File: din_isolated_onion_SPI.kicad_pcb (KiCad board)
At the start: 2 copper layers, 32.5 x 40.5 mm, 38 parts, among them J1 Conn_01x16, J2 Conn_01x16, J3 Conn_01x10, J4 Test_Power_Bridge, U1 Omega2+, U2 SI8661AB-B-IS1, U3 TPL5010-Q1, U4 74LVC125, U5 NL7SZ19

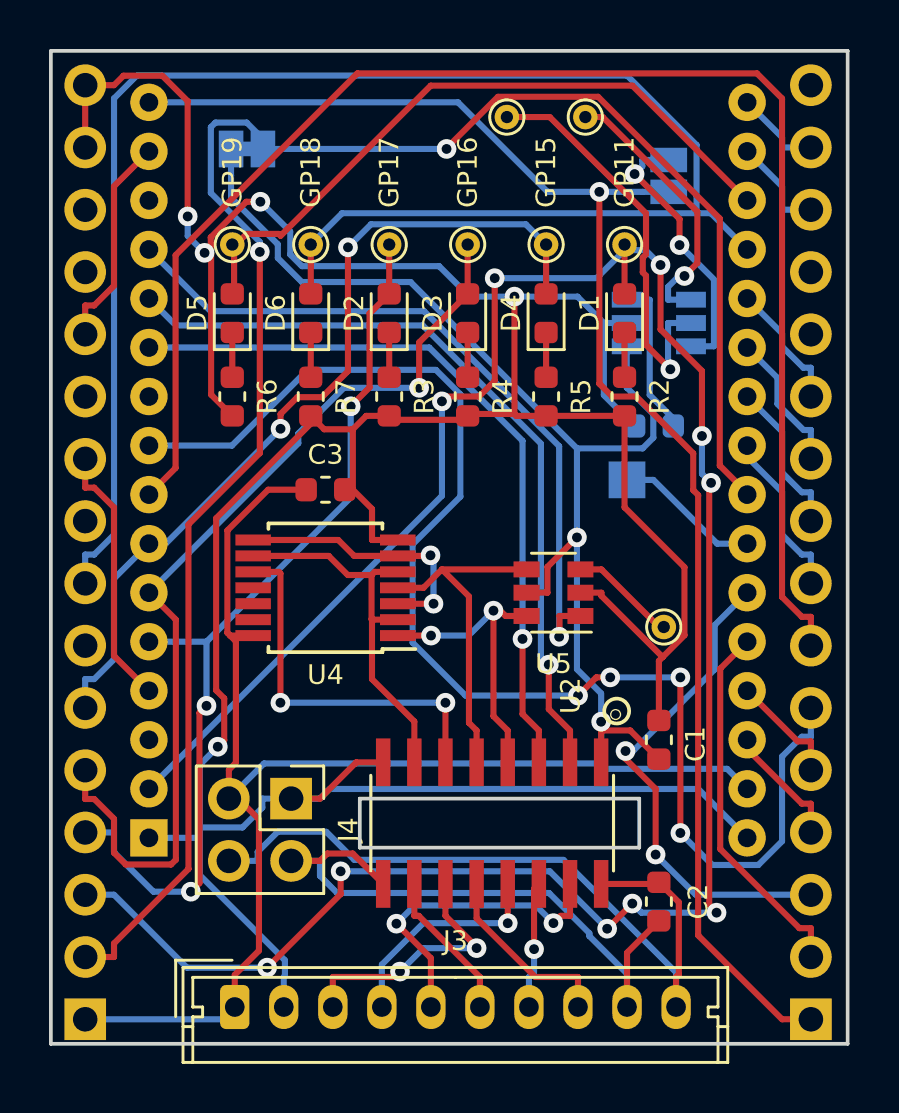
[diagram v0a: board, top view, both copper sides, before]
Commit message: Complete route with x4 layers
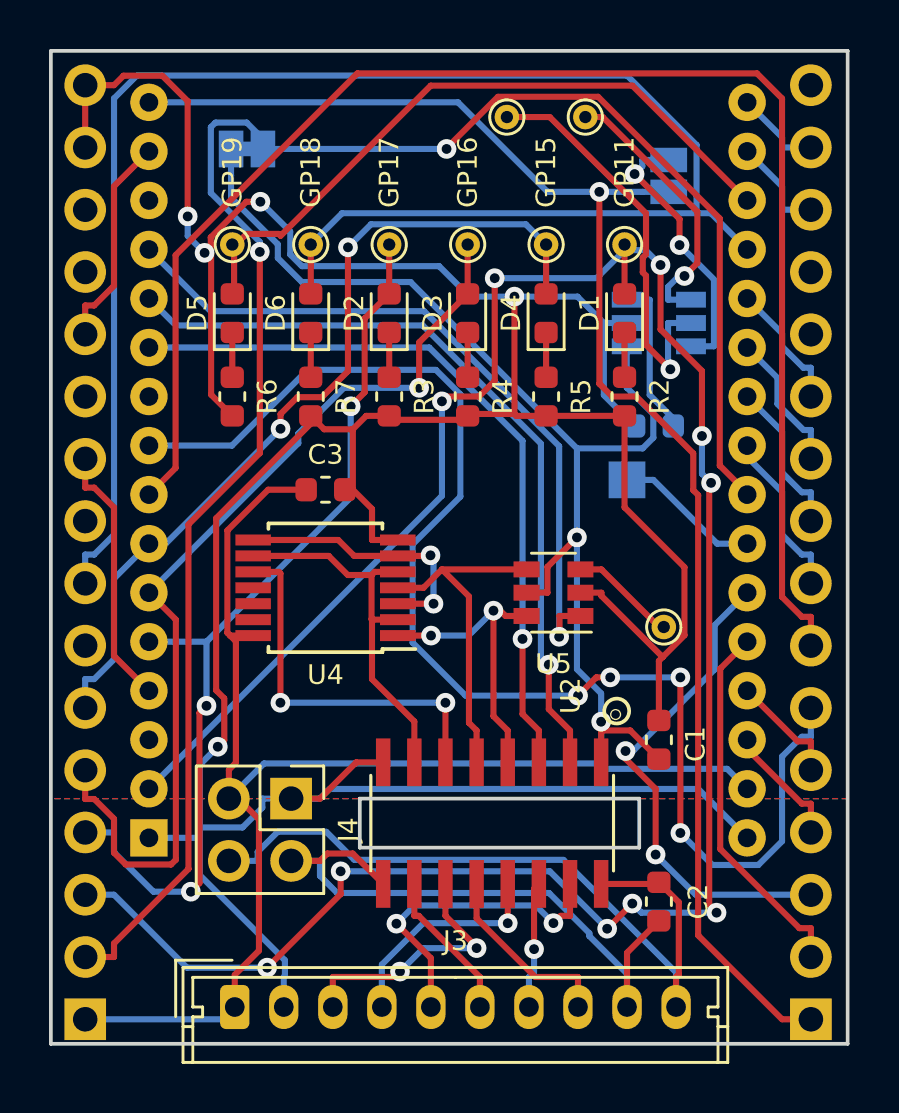
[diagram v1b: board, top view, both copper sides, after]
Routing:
- net /GP19: track 27.7 -> 60.9 mm
- net Net-(J1-Pad9): track 0.00 -> 10.00 mm
- net Net-(J1-Pad11): track 0.00 -> 9.08 mm
- added copper zone on B.Cu, net GND_C
- added copper zone on F.Cu, net GND_C
- added copper zone on In1.Cu, net GND_C
- added copper zone on In2.Cu, net GND_C
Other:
- copper layers 2 -> 4
- board text added: "DIN Onion SPI Isolator http://whatnick.com v0.2 2019-08-24"
- board text removed: "DIN Onion SPI Isolator http://whatnick.com v0.1 2019-06-20"
